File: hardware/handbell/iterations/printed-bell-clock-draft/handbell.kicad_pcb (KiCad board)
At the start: 2 copper layers, 44.5 x 48.3 mm, 104 parts, among them IC1 RP2040_QFN56, IC4 LSM6DSOXTR, J1 504050-0291, J2 SM02B-SRSS-TB, Q1 AO3401, Q2 C20917, Q3 DMG3415UFY, Q4 AO3400A, Q5 CSD83325L, U1 W25Q16JVUXIQ TR / 2MB, U2 RT9080-3.3, U3 MCP73831T-2ACI/OT, U4 MAX98357A, U5 TPS61023DRLR, U6 BQ29700DSER, X6 USB Type C, Y1 12MHz/CL10pF

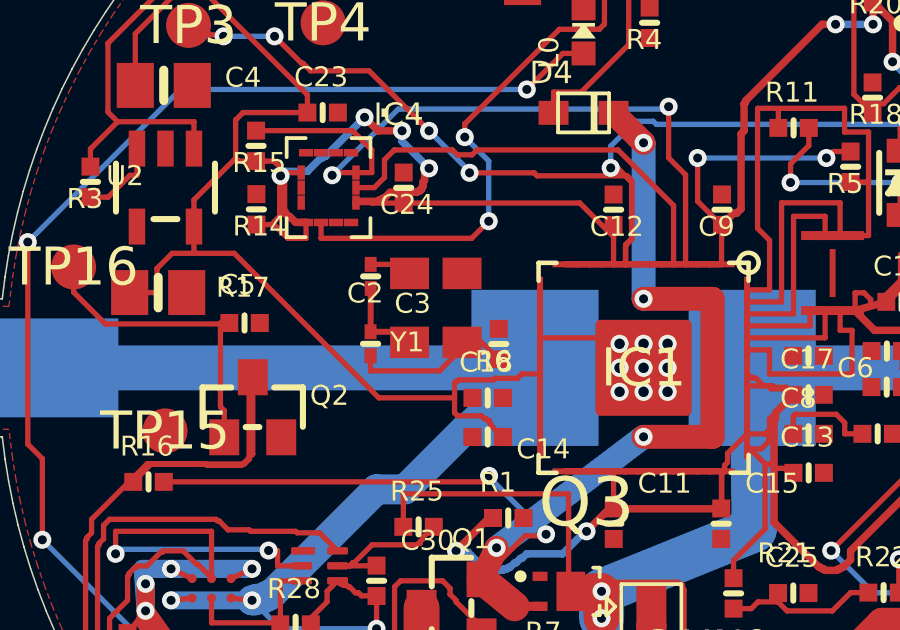
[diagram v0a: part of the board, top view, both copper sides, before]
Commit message: Complete local clock network with all-front signals and returns
Preserve fixed interfaces and nonclock copper; document exact four-part moves, native evidence and two-retry bounded workflow.

Co-authored-by: Copilot <223556219+Copilot@users.noreply.github.com>
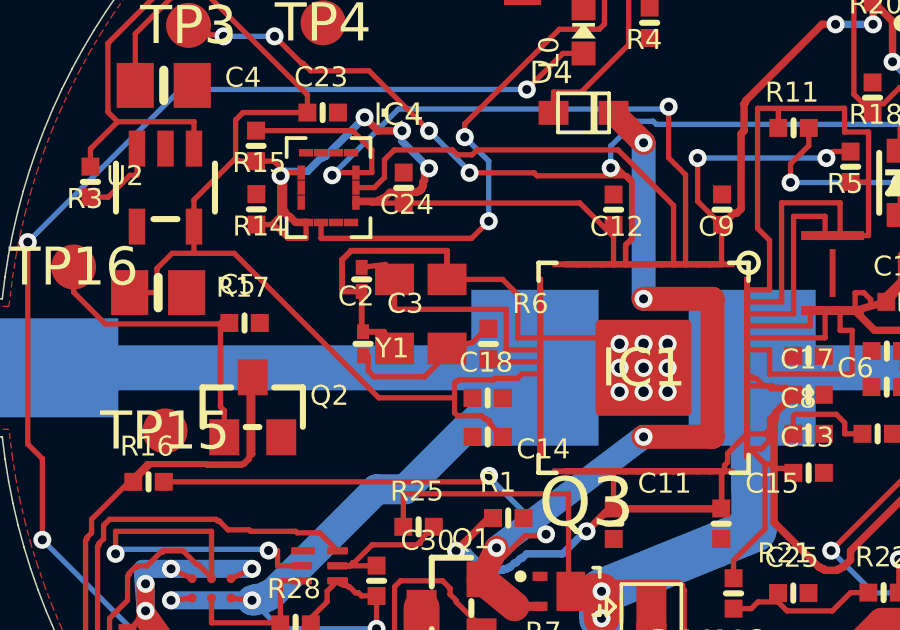
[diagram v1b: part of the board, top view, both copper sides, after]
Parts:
- moved Y1 0.54 mm to (92.6, 98.2)
- moved R6 0.35 mm to (94.8, 99.2), turned to 270 degrees
- moved C2 0.32 mm to (90.6, 97.1)
- moved C3 0.25 mm to (90.6, 99.2)
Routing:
- net GND: track 104.8 -> 115.7 mm
- net Net-(IC1-XIN): track 1.42 -> 8.58 mm
- net Net-(IC1-XOUT): track 0.00 -> 1.76 mm
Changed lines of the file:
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@@
 (net "Net-(IC1-XIN)"))
 	(embedded_fonts no)
-(at 90.903600 96.952450 90)
+(at 90.6036 97.05245 90)
 (property "MPN" "GRM1555C1H150JA01D" (at 0 0 0) (layer "F.Fab") (hide yes) (effects (font (size 1 1))))
 (property "Manufacturer" "Murata" (at 0 0 0) (layer "F.Fab") (hide yes) (effects (font (size 1 1)))))
@@
 (net "Net-(C3-Pad2)"))
 	(embedded_fonts no)
-(at 90.899181 99.199331 270)
+(at 90.649181 99.199331 270)
 (property "MPN" "GRM1555C1H150JA01D" (at 0 0 0) (layer "F.Fab") (hide yes) (effects (font (size 1 1))))
 (property "Manufacturer" "Murata" (at 0 0 0) (layer "F.Fab") (hide yes) (effects (font (size 1 1)))))
@@
 (net "Net-(IC1-XOUT)"))
 	(embedded_fonts no)
-(at 95.175414 99.205901 90)
+(at 94.825414 99.205901 270)
 )
 (footprint "Adafruit Feather RP2040 Prop-Maker-import-fps:_0402NO"
@@
 (net "GND") (pintype "passive") (pinfunction "CASE"))
 	(embedded_fonts no)
-(at 93.074801 98.002596 90)
+(at 92.574801 98.202596 90)
 (fp_rect (start -1.6 -1.25) (end 1.6 1.25) (stroke (width .1) (type solid)) (fill none) (layer "F.Fab"))
 (property "MPN" "ABM8-272-T3" (at 0 0 0) (layer "F.Fab") (hide yes) (effects (font (size 1 1))))
@@
 		)
 	)
-(segment (start 90.9036 96.55245) (end 91.899655 96.55245) (width 0.1778) (layer "F.Cu") (net "Net-(IC1-XIN)"))
-(segment (start 91.899655 96.55245) (end 92.199801 96.852596) (width 0.1778) (layer "F.Cu") (net "Net-(IC1-XIN)"))
-(segment (start 90.899181 99.599331) (end 90.899181 100.1) (width 0.1778) (layer "F.Cu") (net "Net-(C3-Pad2)"))
-(segment (start 90.899181 100.1) (end 93.2 100.1) (width 0.1778) (layer "F.Cu") (net "Net-(C3-Pad2)"))
-(segment (start 93.2 100.1) (end 93.949801 99.350199) (width 0.1778) (layer "F.Cu") (net "Net-(C3-Pad2)"))
-(segment (start 93.949801 99.350199) (end 93.949801 99.152596) (width 0.1778) (layer "F.Cu") (net "Net-(C3-Pad2)"))
-(segment (start 93.949801 99.152596) (end 94.6 99.152596) (width 0.1778) (layer "F.Cu") (net "Net-(C3-Pad2)"))
-(segment (start 94.6 99.152596) (end 95.161305 99.713901) (width 0.1778) (layer "F.Cu") (net "Net-(C3-Pad2)"))
-(segment (start 95.161305 99.713901) (end 95.175414 99.713901) (width 0.1778) (layer "F.Cu") (net "Net-(C3-Pad2)"))
-(segment (start 90.9036 97.35245) (end 90.9036 98.794912) (width 0.2) (layer "F.Cu") (net "GND"))
-(segment (start 90.9036 98.794912) (end 90.899181 98.799331) (width 0.2) (layer "F.Cu") (net "GND"))
-(segment (start 90.899181 98.799331) (end 91.846536 98.799331) (width 0.2) (layer "F.Cu") (net "GND"))
-(segment (start 91.846536 98.799331) (end 92.199801 99.152596) (width 0.2) (layer "F.Cu") (net "GND"))
 (segment (start 96.55 99.0) (end 100.0 99.0) (width 0.1778) (layer "F.Cu") (net "GND"))
-(segment (start 100.0 99.0) (end 100.0 100.0) (width 0.1778) (layer "F.Cu") (net "GND")))
+(segment (start 100.0 99.0) (end 100.0 100.0) (width 0.1778) (layer "F.Cu") (net "GND"))
+(segment (start 90.6036 96.65245) (end 91.399655 96.55245) (width 0.1778) (layer "F.Cu") (net "Net-(IC1-XIN)"))
+(segment (start 91.399655 96.55245) (end 91.699801 97.052596) (width 0.1778) (layer "F.Cu") (net "Net-(IC1-XIN)"))
+(segment (start 90.649181 99.599331) (end 90.82 99.599331) (width 0.1778) (layer "F.Cu") (net "Net-(C3-Pad2)"))
+(segment (start 90.82 99.599331) (end 90.82 100.1) (width 0.1778) (layer "F.Cu") (net "Net-(C3-Pad2)"))
+(segment (start 90.82 100.1) (end 91.02 100.3) (width 0.1778) (layer "F.Cu") (net "Net-(C3-Pad2)"))
+(segment (start 91.02 100.3) (end 92.7 100.3) (width 0.1778) (layer "F.Cu") (net "Net-(C3-Pad2)"))
+(segment (start 92.7 100.3) (end 93.449801 99.550199) (width 0.1778) (layer "F.Cu") (net "Net-(C3-Pad2)"))
+(segment (start 93.449801 99.550199) (end 93.449801 99.352596) (width 0.1778) (layer "F.Cu") (net "Net-(C3-Pad2)"))
+(segment (start 93.449801 99.352596) (end 94.3 99.152596) (width 0.1778) (layer "F.Cu") (net "Net-(C3-Pad2)"))
+(segment (start 94.3 99.152596) (end 94.754695 98.697901) (width 0.1778) (layer "F.Cu") (net "Net-(C3-Pad2)"))
+(segment (start 94.754695 98.697901) (end 94.825414 98.697901) (width 0.1778) (layer "F.Cu") (net "Net-(C3-Pad2)"))
+(segment (start 90.6036 97.45245) (end 90.6036 98.75375) (width 0.2) (layer "F.Cu") (net "GND"))
+(segment (start 90.6036 98.75375) (end 90.649181 98.799331) (width 0.2) (layer "F.Cu") (net "GND"))
+(segment (start 90.649181 98.799331) (end 91.346536 98.799331) (width 0.2) (layer "F.Cu") (net "GND"))
+(segment (start 91.346536 98.799331) (end 91.699801 99.352596) (width 0.2) (layer "F.Cu") (net "GND"))
+(segment (start 91.699801 97.052596) (end 91.699801 98.05) (width 0.1778) (layer "F.Cu") (net "Net-(IC1-XIN)"))
+(segment (start 91.699801 98.05) (end 95.42 98.05) (width 0.1778) (layer "F.Cu") (net "Net-(IC1-XIN)"))
+(segment (start 95.42 98.05) (end 95.42 99.4) (width 0.1778) (layer "F.Cu") (net "Net-(IC1-XIN)"))
+(segment (start 95.42 99.4) (end 96.55 99.4) (width 0.1778) (layer "F.Cu") (net "Net-(IC1-XIN)"))
+(segment (start 96.55 99.8) (end 94.911513 99.8) (width 0.1778) (layer "F.Cu") (net "Net-(IC1-XOUT)"))
+(segment (start 94.911513 99.8) (end 94.825414 99.713901) (width 0.1778) (layer "F.Cu") (net "Net-(IC1-XOUT)"))
+(segment (start 90.6036 97.45245) (end 89.95 97.45245) (width 0.2) (layer "F.Cu") (net "GND"))
+(segment (start 89.95 97.45245) (end 89.95 96.4) (width 0.2) (layer "F.Cu") (net "GND"))
+(segment (start 89.95 96.4) (end 90.25 96.1) (width 0.2) (layer "F.Cu") (net "GND"))
+(segment (start 90.25 96.1) (end 93.449801 96.1) (width 0.2) (layer "F.Cu") (net "GND"))
+(segment (start 93.449801 96.1) (end 93.449801 97.052596) (width 0.2) (layer "F.Cu") (net "GND"))
+(segment (start 93.449801 97.052596) (end 95.3 97.052596) (width 0.1778) (layer "F.Cu") (net "GND"))
+(segment (start 95.3 97.052596) (end 95.81 97.562596) (width 0.1778) (layer "F.Cu") (net "GND"))
+(segment (start 95.81 97.562596) (end 95.81 99.0) (width 0.1778) (layer "F.Cu") (net "GND"))
+(segment (start 95.81 99.0) (end 96.55 99.0) (width 0.1778) (layer "F.Cu") (net "GND")))

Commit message: Apply selected Q3 identity while retaining corrected native geometry
Preserve circuitry, copper and placements; publish scoped native identity and schematic evidence.

Co-authored-by: Copilot <223556219+Copilot@users.noreply.github.com>
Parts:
- Q3: value DMG3415UFY -> DMP2045UFY4
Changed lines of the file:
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@@
 		)
 )
-	(property "Value" "DMG3415UFY"
+	(property "Value" "DMP2045UFY4"
 		(at -1 4 0)
 		(layer "F.Fab")
@@
 		)
 )
-	(property "Datasheet" ""
+	(property "Datasheet" "https://www.diodes.com/datasheet/download/DMP2045UFY4.pdf"
 		(at 0 0 0)
 		(layer "F.Fab")
@@
 		)
 )
-	(property "Description" ""
+	(property "Description" "P-channel MOSFET; X2-DFN2015-3; G=1, S=2, D=3. Selected replacement, not electrically identical."
 		(at 0 0 0)
 		(layer "F.Fab")
@@
 )
 (at 97.500000 107.450000 0)
-)
+(property "MPN" "DMP2045UFY4-7" (at 0 0 0) (layer "F.Fab") (hide yes) (effects (font (size 1 1))))
+(property "Manufacturer" "Diodes Incorporated" (at 0 0 0) (layer "F.Fab") (hide yes) (effects (font (size 1 1)))))
 (footprint "Package_TO_SOT_SMD:SOT-23"
 	(layer "F.Cu")
